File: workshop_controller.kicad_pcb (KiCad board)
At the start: 2 copper layers, 15 parts, among them J1 Conn_02x10_Odd_Even, J2 Conn_02x10_Odd_Even, J3 AudioJack3, J5 Conn_02x25_Odd_Even, U1 MPU-9250, U2 BME280, U3 MCP23S17_SS, U4 LM4990MM

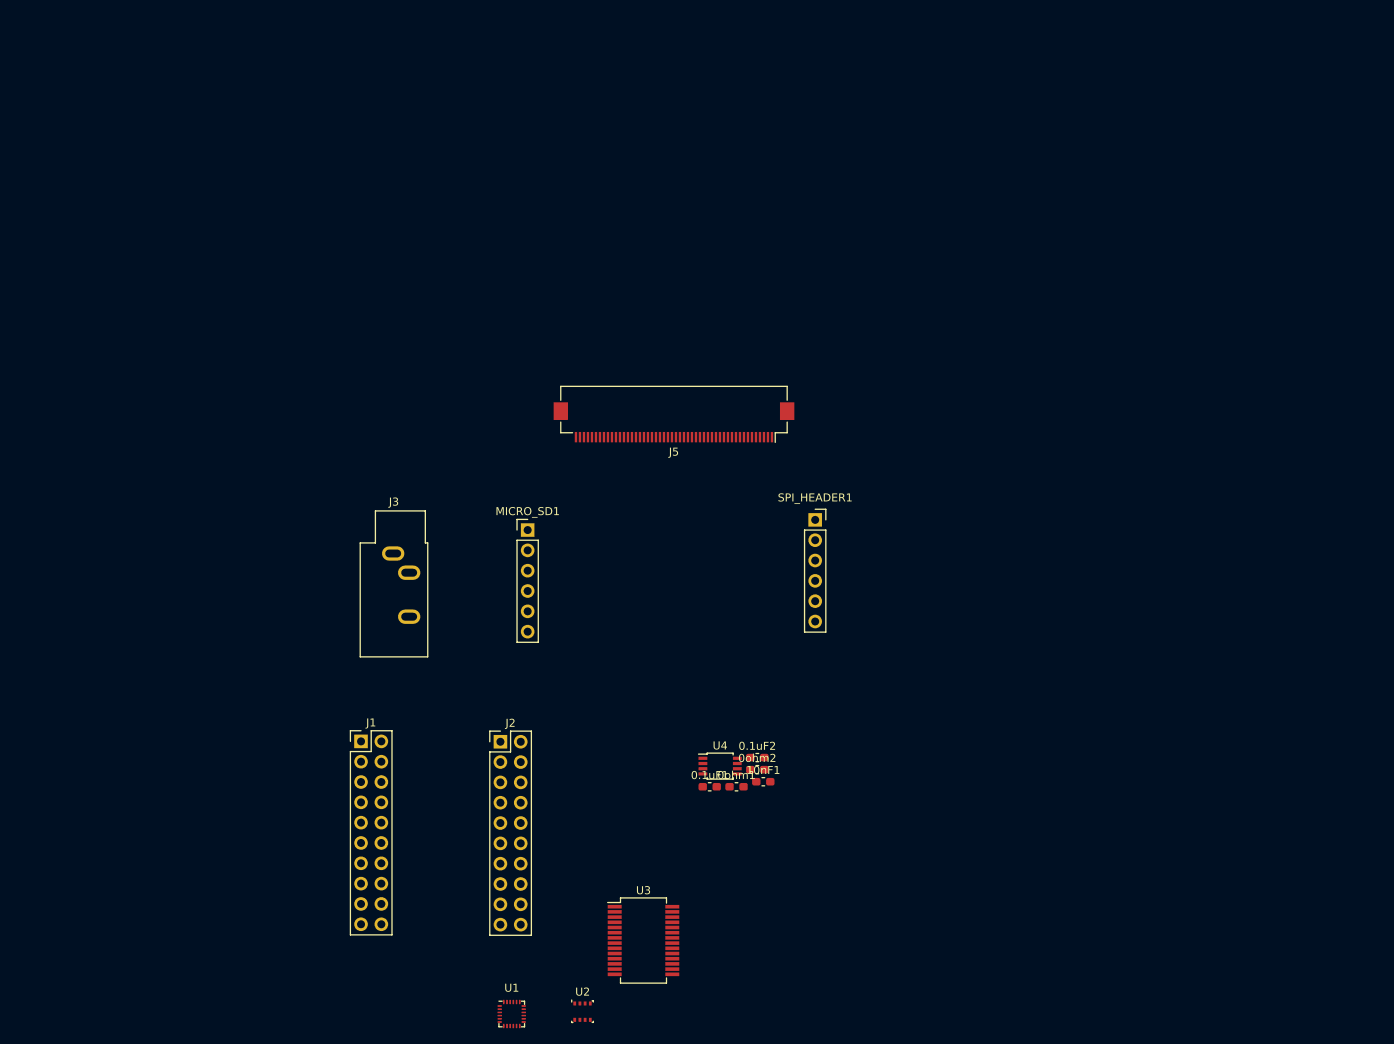
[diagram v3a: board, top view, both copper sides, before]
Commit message: add outline
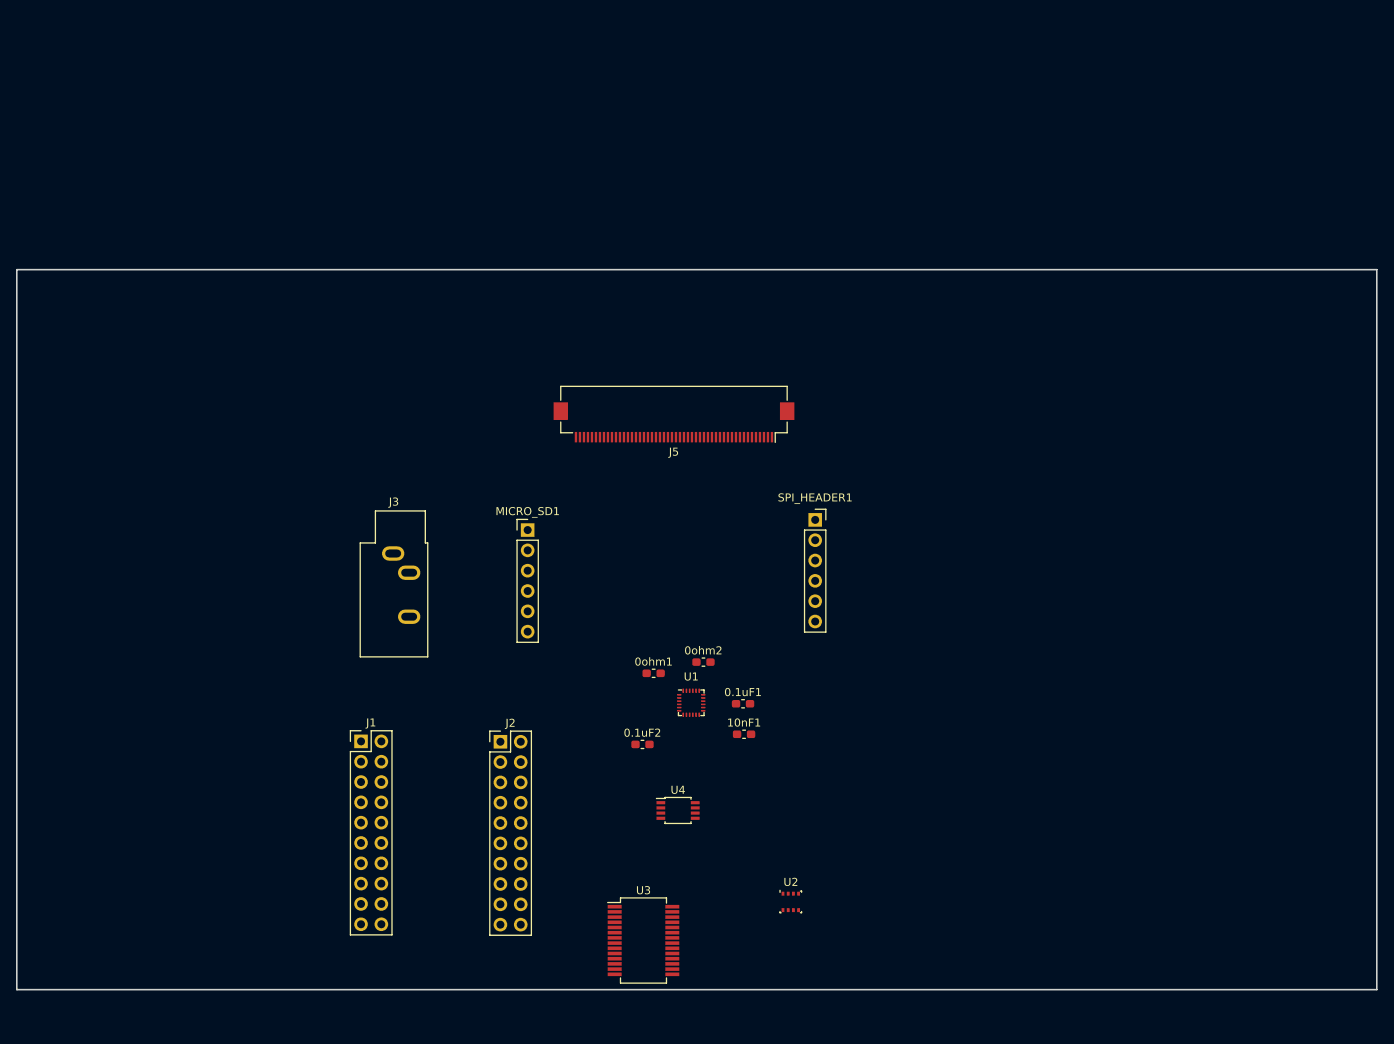
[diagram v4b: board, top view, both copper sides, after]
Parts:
- moved U1 44.9 mm to (154.3, 104.1)
- moved U2 29.4 mm to (166.8, 129.0)
- moved 0ohm1 17.6 mm to (149.6, 100.5)
- moved 0ohm2 15.0 mm to (155.8, 99.1)
- moved 0.1uF2 14.4 mm to (148.2, 109.3)
- moved 0.1uF1 11.2 mm to (160.8, 104.3)
- moved U4 7.64 mm to (152.7, 117.6)
- moved 10nF1 6.40 mm to (160.9, 108.1)
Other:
- board outline added: 170 x 90 mm
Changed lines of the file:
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@@
   (general
     (thickness 1.6)
-    (drawings 0)
+    (drawings 4)
     (tracks 0)
     (zones 0)
@@
   )
   (module Sensor_Motion:InvenSense_QFN-24_3x3mm_P0.4mm (layer F.Cu)
-    (at 131.869001 143.045001)
+    (at 154.305 104.14)
     (descr "24-Lead Plastic QFN (3mm x 3mm); Pitch 0.4mm; EP 1.7x1.54mm; for InvenSense motion sensors; keepout area marked (Package see: https://store.invensense.com/datasheets/invensense/MPU9250REV1.0.pdf; See also https://www.invensense.com/wp-content/uploads/2015/02/InvenSense-MEMS-Handling.pdf)")
     (tags "QFN 0.4")
@@
   )
   (module Package_LGA:Bosch_LGA-8_2.5x2.5mm_P0.65mm_ClockwisePinNumbering (layer F.Cu)
-    (at 140.716 142.748)
+    (at 166.751 129.032)
     (descr LGA-8)
     (tags "lga land grid array")
@@
   )
   (module Capacitor_SMD:C_0603_1608Metric_Pad1.05x0.95mm_HandSolder (layer F.Cu)
-    (at 156.615001 114.641001)
+    (at 160.782 104.267)
     (descr "Capacitor SMD 0603 (1608 Metric), square (rectangular) end terminal, IPC_7351 nominal with elongated pad for handsoldering. (Body size source: http://www.tortai-tech.com/upload/download/2011102023233369053.pdf), generated with kicad-footprint-generator")
     (tags "capacitor handsolder")
@@
   )
   (module Capacitor_SMD:C_0603_1608Metric_Pad1.05x0.95mm_HandSolder (layer F.Cu)
-    (at 162.565001 110.991001)
+    (at 148.209 109.347)
     (descr "Capacitor SMD 0603 (1608 Metric), square (rectangular) end terminal, IPC_7351 nominal with elongated pad for handsoldering. (Body size source: http://www.tortai-tech.com/upload/download/2011102023233369053.pdf), generated with kicad-footprint-generator")
     (tags "capacitor handsolder")
@@
   )
   (module Resistor_SMD:R_0603_1608Metric_Pad1.05x0.95mm_HandSolder (layer F.Cu)
-    (at 159.965001 114.641001)
+    (at 149.606 100.457)
     (descr "Resistor SMD 0603 (1608 Metric), square (rectangular) end terminal, IPC_7351 nominal with elongated pad for handsoldering. (Body size source: http://www.tortai-tech.com/upload/download/2011102023233369053.pdf), generated with kicad-footprint-generator")
     (tags "resistor handsolder")
@@
   )
   (module Resistor_SMD:R_0603_1608Metric_Pad1.05x0.95mm_HandSolder (layer F.Cu)
-    (at 162.565001 112.501001)
+    (at 155.829 99.06)
     (descr "Resistor SMD 0603 (1608 Metric), square (rectangular) end terminal, IPC_7351 nominal with elongated pad for handsoldering. (Body size source: http://www.tortai-tech.com/upload/download/2011102023233369053.pdf), generated with kicad-footprint-generator")
     (tags "resistor handsolder")
@@
   )
   (module Capacitor_SMD:C_0603_1608Metric_Pad1.05x0.95mm_HandSolder (layer F.Cu)
-    (at 163.315001 114.011001)
+    (at 160.909 108.077)
     (descr "Capacitor SMD 0603 (1608 Metric), square (rectangular) end terminal, IPC_7351 nominal with elongated pad for handsoldering. (Body size source: http://www.tortai-tech.com/upload/download/2011102023233369053.pdf), generated with kicad-footprint-generator")
     (tags "capacitor handsolder")
@@
   )
   (module Package_SO:TSSOP-8_3x3mm_P0.65mm (layer F.Cu)
-    (at 157.915001 112.061001)
+    (at 152.654 117.602)
     (descr "TSSOP8: plastic thin shrink small outline package; 8 leads; body width 3 mm; (see NXP SSOP-TSSOP-VSO-REFLOW.pdf and sot505-1_po.pdf)")
     (tags "SSOP 0.65")
@@
     )
   )
+  (gr_line (start 70 50) (end 240 50) (layer Edge.Cuts) (width 0.2))
+  (gr_line (start 70 140) (end 70 50) (layer Edge.Cuts) (width 0.2))
+  (gr_line (start 240 140) (end 70 140) (layer Edge.Cuts) (width 0.2))
+  (gr_line (start 240 50) (end 240 140) (layer Edge.Cuts) (width 0.2))
 )

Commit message: Add labels
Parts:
- added 0ohm3: R_Small, Resistor_SMD:R_0603_1608Metric_Pad1.05x0.95mm_HandSolder, F.Cu at (146.5, 84.6)
- added 0ohm4: R_Small, Resistor_SMD:R_0603_1608Metric_Pad1.05x0.95mm_HandSolder, F.Cu at (146.5, 87.1)
- added C1: 100nF, Capacitor_SMD:C_0603_1608Metric_Pad1.05x0.95mm_HandSolder, F.Cu at (150.8, 84.6)
- added C2: 100nF, Capacitor_SMD:C_0603_1608Metric_Pad1.05x0.95mm_HandSolder, F.Cu at (150.8, 87.1)
- added J4: Micro_SD_Card, Connector_Card:microSD_HC_Wuerth_693072010801, F.Cu at (88.1, 62.0)
- added R1: 4.7kohm, Resistor_SMD:R_0603_1608Metric_Pad1.05x0.95mm_HandSolder, F.Cu at (155.2, 84.6)
- added R2: 4.7kohm, Resistor_SMD:R_0603_1608Metric_Pad1.05x0.95mm_HandSolder, F.Cu at (155.2, 87.1)
- added R3: 50kOhm, Resistor_SMD:R_1206_3216Metric_Pad1.42x1.75mm_HandSolder, F.Cu at (107.3, 60.8)
- added R4: 50kOhm, Resistor_SMD:R_1206_3216Metric_Pad1.42x1.75mm_HandSolder, F.Cu at (107.3, 64.1)
- added R5: 50kOhm, Resistor_SMD:R_1206_3216Metric_Pad1.42x1.75mm_HandSolder, F.Cu at (114.5, 60.8)
- added R6: 50kOhm, Resistor_SMD:R_1206_3216Metric_Pad1.42x1.75mm_HandSolder, F.Cu at (107.3, 67.4)
- added R7: 50kOhm, Resistor_SMD:R_1206_3216Metric_Pad1.42x1.75mm_HandSolder, F.Cu at (114.5, 64.1)
- added SW1: SW_Push, Button_Switch_THT:SW_PUSH-12mm_Wuerth-430476085716, F.Cu at (194.8, 81.2)
- added SW2: SW_Push, Button_Switch_THT:SW_PUSH-12mm_Wuerth-430476085716, F.Cu at (194.8, 98.6)
- added SW3: SW_Push, Button_Switch_THT:SW_PUSH-12mm_Wuerth-430476085716, F.Cu at (215.7, 81.2)
- added SW4: SW_Push, Button_Switch_THT:SW_PUSH-12mm_Wuerth-430476085716, F.Cu at (215.7, 98.6)
- C3: renamed from 0.1uF2; value C_Small -> 0.1µF
- C4: renamed from 10nF1; value C_Small -> 10nF
- C5: renamed from 0.1uF1; value C_Small -> 0.1µF
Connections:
- net /PIN_27 renamed /I2C_SCK
- net /PIN_TXD renamed Net-(J2-Pad1)
- J2 pad 6: /PIN_25 -> Net-(J2-Pad6)
- J2 pad 8: /PIN_32 -> /I2C_SDA
- J5 pad 38: /PIN_CS -> /PIN_4
- SPI_HEADER1 pad 2: Net-(SPI_HEADER1-Pad2) -> /PIN_34
- U1 pad 24: /PIN_25 -> /I2C_SDA
- U2 pad 2: Net-(U2-Pad2) -> +3V3
- U2 pad 3: /PIN_25 -> /I2C_SDA
- U2 pad 8: +3V3 -> Net-(C2-Pad2)
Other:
- outline, holes or cut-outs redrawn

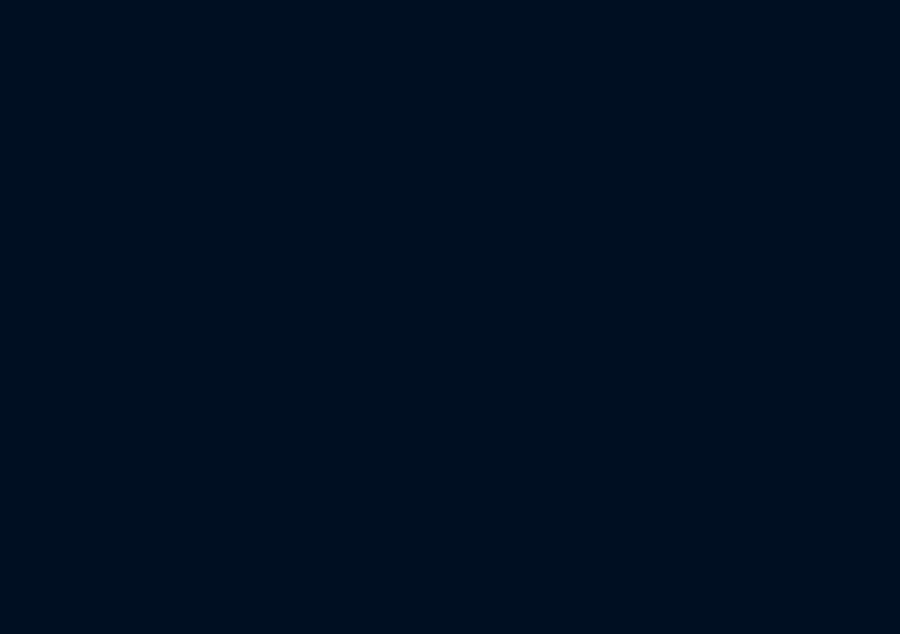
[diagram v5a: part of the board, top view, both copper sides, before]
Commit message: Add opamp for mic preamp
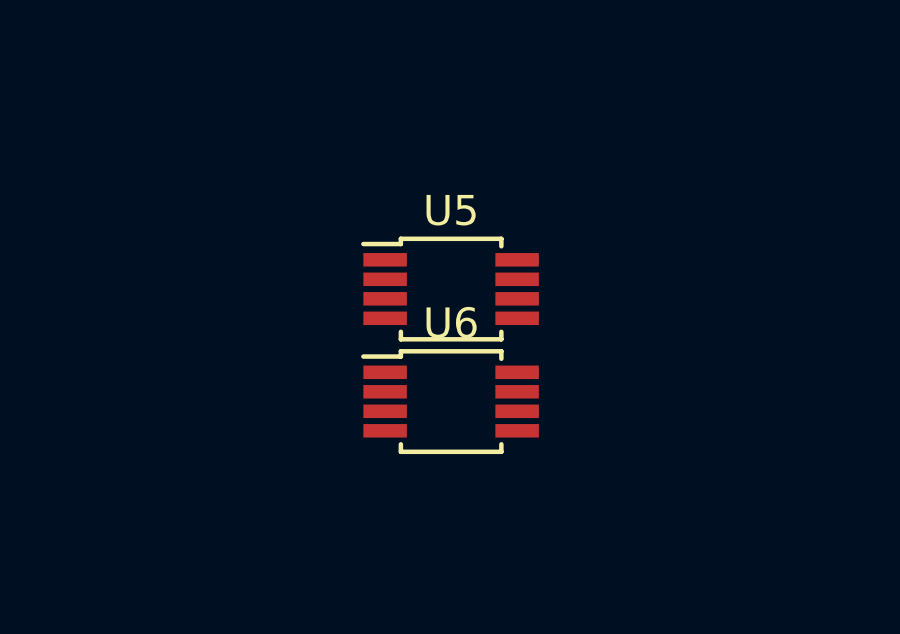
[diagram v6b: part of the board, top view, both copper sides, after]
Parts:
- added U5: LM358, Package_SO:MSOP-8_3x3mm_P0.65mm, F.Cu at (185.7, 61.6)
- added U6: LM358, Package_SO:MSOP-8_3x3mm_P0.65mm, F.Cu at (185.7, 65.4)
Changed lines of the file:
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@@
-(kicad_pcb (version 20171130) (host pcbnew "(5.1.0)-1")
+(kicad_pcb (version 20171130) (host pcbnew 5.0.2-bee76a0~70~ubuntu18.04.1)
   (general
     (thickness 1.6)
@@
     (tracks 0)
     (zones 0)
-    (modules 31)
-    (nets 131)
+    (modules 33)
+    (nets 139)
   )
   (page A4)
@@
     (zone_45_only no)
     (trace_min 0.2)
+    (segment_width 0.2)
+    (edge_width 0.15)
     (via_size 0.8)
     (via_drill 0.4)
@@
     (uvia_min_size 0.2)
     (uvia_min_drill 0.1)
-    (edge_width 0.15)
-    (segment_width 0.2)
     (pcb_text_width 0.3)
     (pcb_text_size 1.5 1.5)
@@
   (net 129 "Net-(J4-Pad1)")
   (net 130 "Net-(J2-Pad1)")
+  (net 131 "Net-(U5-Pad3)")
+  (net 132 "Net-(U5-Pad2)")
+  (net 133 "Net-(U5-Pad1)")
+  (net 134 "Net-(U6-Pad4)")
+  (net 135 "Net-(U6-Pad5)")
+  (net 136 "Net-(U6-Pad6)")
+  (net 137 "Net-(U6-Pad7)")
+  (net 138 "Net-(U6-Pad8)")
   (net_class Default "This is the default net class."
     (clearance 0.2)
@@
     (add_net "Net-(U4-Pad7)")
     (add_net "Net-(U4-Pad8)")
+    (add_net "Net-(U5-Pad1)")
+    (add_net "Net-(U5-Pad2)")
+    (add_net "Net-(U5-Pad3)")
+    (add_net "Net-(U6-Pad4)")
+    (add_net "Net-(U6-Pad5)")
+    (add_net "Net-(U6-Pad6)")
+    (add_net "Net-(U6-Pad7)")
+    (add_net "Net-(U6-Pad8)")
   )
   (module Sensor_Motion:InvenSense_QFN-24_3x3mm_P0.4mm (layer F.Cu)
@@
       (at (xyz 0 0 0))
       (scale (xyz 1 1 1))
+      (rotate (xyz 0 0 0))
+    )
+  )
+  (module Package_SO:MSOP-8_3x3mm_P0.65mm (layer F.Cu)
+    (at 185.725001 61.625001)
+    (descr "8-Lead Plastic Micro Small Outline Package (MS) [MSOP] (see Microchip Packaging Specification 00000049BS.pdf)")
+    (tags "SSOP 0.65")
+    (attr smd)
+    (fp_text reference U5 (at 0 -2.6) (layer F.SilkS)
+      (effects (font (size 1 1) (thickness 0.15)))
+    )
+    (fp_text value LM358 (at 0 2.6) (layer F.Fab)
+      (effects (font (size 1 1) (thickness 0.15)))
+    )
+    (fp_text user %R (at 0 0) (layer F.Fab)
+      (effects (font (size 0.6 0.6) (thickness 0.15)))
+    )
+    (fp_line (start -1.675 -1.5) (end -2.925 -1.5) (layer F.SilkS) (width 0.15))
+    (fp_line (start -1.675 1.675) (end 1.675 1.675) (layer F.SilkS) (width 0.15))
+    (fp_line (start -1.675 -1.675) (end 1.675 -1.675) (layer F.SilkS) (width 0.15))
+    (fp_line (start -1.675 1.675) (end -1.675 1.425) (layer F.SilkS) (width 0.15))
+    (fp_line (start 1.675 1.675) (end 1.675 1.425) (layer F.SilkS) (width 0.15))
+    (fp_line (start 1.675 -1.675) (end 1.675 -1.425) (layer F.SilkS) (width 0.15))
+    (fp_line (start -1.675 -1.675) (end -1.675 -1.5) (layer F.SilkS) (width 0.15))
+    (fp_line (start -3.2 1.85) (end 3.2 1.85) (layer F.CrtYd) (width 0.05))
+    (fp_line (start -3.2 -1.85) (end 3.2 -1.85) (layer F.CrtYd) (width 0.05))
+    (fp_line (start 3.2 -1.85) (end 3.2 1.85) (layer F.CrtYd) (width 0.05))
+    (fp_line (start -3.2 -1.85) (end -3.2 1.85) (layer F.CrtYd) (width 0.05))
+    (fp_line (start -1.5 -0.5) (end -0.5 -1.5) (layer F.Fab) (width 0.15))
+    (fp_line (start -1.5 1.5) (end -1.5 -0.5) (layer F.Fab) (width 0.15))
+    (fp_line (start 1.5 1.5) (end -1.5 1.5) (layer F.Fab) (width 0.15))
+    (fp_line (start 1.5 -1.5) (end 1.5 1.5) (layer F.Fab) (width 0.15))
+    (fp_line (start -0.5 -1.5) (end 1.5 -1.5) (layer F.Fab) (width 0.15))
+    (pad 8 smd rect (at 2.2 -0.975) (size 1.45 0.45) (layers F.Cu F.Paste F.Mask))
+    (pad 7 smd rect (at 2.2 -0.325) (size 1.45 0.45) (layers F.Cu F.Paste F.Mask))
+    (pad 6 smd rect (at 2.2 0.325) (size 1.45 0.45) (layers F.Cu F.Paste F.Mask))
+    (pad 5 smd rect (at 2.2 0.975) (size 1.45 0.45) (layers F.Cu F.Paste F.Mask))
+    (pad 4 smd rect (at -2.2 0.975) (size 1.45 0.45) (layers F.Cu F.Paste F.Mask))
+    (pad 3 smd rect (at -2.2 0.325) (size 1.45 0.45) (layers F.Cu F.Paste F.Mask)
+      (net 131 "Net-(U5-Pad3)"))
+    (pad 2 smd rect (at -2.2 -0.325) (size 1.45 0.45) (layers F.Cu F.Paste F.Mask)
+      (net 132 "Net-(U5-Pad2)"))
+    (pad 1 smd rect (at -2.2 -0.975) (size 1.45 0.45) (layers F.Cu F.Paste F.Mask)
+      (net 133 "Net-(U5-Pad1)"))
+    (model ${KISYS3DMOD}/Package_SO.3dshapes/MSOP-8_3x3mm_P0.65mm.wrl
+      (at (xyz 0 0 0))
+      (scale (xyz 1 1 1))
+      (rotate (xyz 0 0 0))
+    )
+  )
+  (module Package_SO:MSOP-8_3x3mm_P0.65mm (layer F.Cu)
+    (at 185.725001 65.375001)
+    (descr "8-Lead Plastic Micro Small Outline Package (MS) [MSOP] (see Microchip Packaging Specification 00000049BS.pdf)")
+    (tags "SSOP 0.65")
+    (attr smd)
+    (fp_text reference U6 (at 0 -2.6) (layer F.SilkS)
+      (effects (font (size 1 1) (thickness 0.15)))
+    )
+    (fp_text value LM358 (at 0 2.6) (layer F.Fab)
+      (effects (font (size 1 1) (thickness 0.15)))
+    )
+    (fp_line (start -0.5 -1.5) (end 1.5 -1.5) (layer F.Fab) (width 0.15))
+    (fp_line (start 1.5 -1.5) (end 1.5 1.5) (layer F.Fab) (width 0.15))
+    (fp_line (start 1.5 1.5) (end -1.5 1.5) (layer F.Fab) (width 0.15))
+    (fp_line (start -1.5 1.5) (end -1.5 -0.5) (layer F.Fab) (width 0.15))
+    (fp_line (start -1.5 -0.5) (end -0.5 -1.5) (layer F.Fab) (width 0.15))
+    (fp_line (start -3.2 -1.85) (end -3.2 1.85) (layer F.CrtYd) (width 0.05))
+    (fp_line (start 3.2 -1.85) (end 3.2 1.85) (layer F.CrtYd) (width 0.05))
+    (fp_line (start -3.2 -1.85) (end 3.2 -1.85) (layer F.CrtYd) (width 0.05))
+    (fp_line (start -3.2 1.85) (end 3.2 1.85) (layer F.CrtYd) (width 0.05))
+    (fp_line (start -1.675 -1.675) (end -1.675 -1.5) (layer F.SilkS) (width 0.15))
+    (fp_line (start 1.675 -1.675) (end 1.675 -1.425) (layer F.SilkS) (width 0.15))
+    (fp_line (start 1.675 1.675) (end 1.675 1.425) (layer F.SilkS) (width 0.15))
+    (fp_line (start -1.675 1.675) (end -1.675 1.425) (layer F.SilkS) (width 0.15))
+    (fp_line (start -1.675 -1.675) (end 1.675 -1.675) (layer F.SilkS) (width 0.15))
+    (fp_line (start -1.675 1.675) (end 1.675 1.675) (layer F.SilkS) (width 0.15))
+    (fp_line (start -1.675 -1.5) (end -2.925 -1.5) (layer F.SilkS) (width 0.15))
+    (fp_text user %R (at 0 0) (layer F.Fab)
+      (effects (font (size 0.6 0.6) (thickness 0.15)))
+    )
+    (pad 1 smd rect (at -2.2 -0.975) (size 1.45 0.45) (layers F.Cu F.Paste F.Mask))
+    (pad 2 smd rect (at -2.2 -0.325) (size 1.45 0.45) (layers F.Cu F.Paste F.Mask))
+    (pad 3 smd rect (at -2.2 0.325) (size 1.45 0.45) (layers F.Cu F.Paste F.Mask))
+    (pad 4 smd rect (at -2.2 0.975) (size 1.45 0.45) (layers F.Cu F.Paste F.Mask)
+      (net 134 "Net-(U6-Pad4)"))
+    (pad 5 smd rect (at 2.2 0.975) (size 1.45 0.45) (layers F.Cu F.Paste F.Mask)
+      (net 135 "Net-(U6-Pad5)"))
+    (pad 6 smd rect (at 2.2 0.325) (size 1.45 0.45) (layers F.Cu F.Paste F.Mask)
+      (net 136 "Net-(U6-Pad6)"))
+    (pad 7 smd rect (at 2.2 -0.325) (size 1.45 0.45) (layers F.Cu F.Paste F.Mask)
+      (net 137 "Net-(U6-Pad7)"))
+    (pad 8 smd rect (at 2.2 -0.975) (size 1.45 0.45) (layers F.Cu F.Paste F.Mask)
+      (net 138 "Net-(U6-Pad8)"))
+    (model ${KISYS3DMOD}/Package_SO.3dshapes/MSOP-8_3x3mm_P0.65mm.wrl
+      (at (xyz 0 0 0))
+      (scale (xyz 1 1 1))
